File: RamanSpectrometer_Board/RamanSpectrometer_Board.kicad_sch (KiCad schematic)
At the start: 35 parts, among them J1 RJ45_LED_Shielded, Q1 BSS138, Q2 BSS138, Q3 BSS138, Q4 BSS138, Q5 BSS138, U1 Teensy4.1_DEV-16771, U2 OKI, U3 OKI

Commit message: footprints
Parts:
- C2, C3, C4, C5: footprint (none) -> Capacitor_SMD:C_0603_1608Metric_Pad1.08x0.95mm_HandSolder
- Conn1: footprint (none) -> MRDT_Connectors:Square_Anderson_2_H_Side_By_Side_PV
- Conn2, Conn4: footprint (none) -> MRDT_Connectors:MOLEX_SL_05_Vertical
- Conn3: footprint (none) -> MRDT_Connectors:MOLEX_SL_03_Vertical
- Conn5: footprint (none) -> MRDT_Connectors:MOLEX_SL_02_Vertical
- D1, D2, D3: footprint (none) -> LED_SMD:LED_0603_1608Metric_Pad1.05x0.95mm_HandSolder
- J1: footprint (none) -> MRDT_Connectors:RJ45_Teensy
- R1, R10, R2, R3, R5, R6, R8: footprint (none) -> Resistor_SMD:R_0603_1608Metric_Pad0.98x0.95mm_HandSolder
- U2, U3: footprint (none) -> MRDT_Devices:OKI_Horizontal
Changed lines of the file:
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@@
 			)
 		)
-		(property "Footprint" ""
+		(property "Footprint" "MRDT_Devices:OKI_Horizontal"
 			(at 66.04 35.56 0)
 			(effects
@@
 			)
 		)
-		(property "Footprint" ""
+		(property "Footprint" "Resistor_SMD:R_0603_1608Metric_Pad0.98x0.95mm_HandSolder"
 			(at 171.45 80.518 90)
 			(effects
@@
 			)
 		)
-		(property "Footprint" ""
+		(property "Footprint" "MRDT_Devices:OKI_Horizontal"
 			(at 120.65 168.91 0)
 			(effects
@@
 			)
 		)
-		(property "Footprint" ""
+		(property "Footprint" "LED_SMD:LED_0603_1608Metric_Pad1.05x0.95mm_HandSolder"
 			(at 128.27 36.83 0)
 			(effects
@@
 			)
 		)
-		(property "Footprint" ""
+		(property "Footprint" "Capacitor_SMD:C_0603_1608Metric_Pad1.08x0.95mm_HandSolder"
 			(at 145.7452 172.72 0)
 			(effects
@@
 			)
 		)
-		(property "Footprint" ""
+		(property "Footprint" "Resistor_SMD:R_0603_1608Metric_Pad0.98x0.95mm_HandSolder"
 			(at 130.81 80.518 90)
 			(effects
@@
 			)
 		)
-		(property "Footprint" ""
+		(property "Footprint" "Capacitor_SMD:C_0603_1608Metric_Pad1.08x0.95mm_HandSolder"
 			(at 63.1952 39.37 0)
 			(effects
@@
 			)
 		)
-		(property "Footprint" ""
+		(property "Footprint" "MRDT_Connectors:MOLEX_SL_03_Vertical"
 			(at 130.81 134.62 0)
 			(effects
@@
 			)
 		)
-		(property "Footprint" ""
+		(property "Footprint" "Resistor_SMD:R_0603_1608Metric_Pad0.98x0.95mm_HandSolder"
 			(at 116.332 49.53 90)
 			(effects
@@
 			)
 		)
-		(property "Footprint" ""
+		(property "Footprint" "MRDT_Connectors:RJ45_Teensy"
 			(at 234.95 34.925 90)
 			(effects
@@
 			)
 		)
-		(property "Footprint" ""
+		(property "Footprint" "Resistor_SMD:R_0603_1608Metric_Pad0.98x0.95mm_HandSolder"
 			(at 136.652 49.53 90)
 			(effects
@@
 			)
 		)
-		(property "Footprint" ""
+		(property "Footprint" "MRDT_Connectors:MOLEX_SL_05_Vertical"
 			(at 180.34 43.18 0)
 			(effects
@@
 			)
 		)
-		(property "Footprint" ""
+		(property "Footprint" "Capacitor_SMD:C_0603_1608Metric_Pad1.08x0.95mm_HandSolder"
 			(at 117.8052 172.72 0)
 			(effects
@@
 			)
 		)
-		(property "Footprint" ""
+		(property "Footprint" "LED_SMD:LED_0603_1608Metric_Pad1.05x0.95mm_HandSolder"
 			(at 138.43 36.83 0)
 			(effects
@@
 			)
 		)
-		(property "Footprint" ""
+		(property "Footprint" "MRDT_Connectors:Square_Anderson_2_H_Side_By_Side_PV"
 			(at 20.32 53.34 0)
 			(effects
@@
 			)
 		)
-		(property "Footprint" ""
+		(property "Footprint" "MRDT_Connectors:MOLEX_SL_02_Vertical"
 			(at 220.98 120.65 0)
 			(effects
@@
 			)
 		)
-		(property "Footprint" ""
+		(property "Footprint" "MRDT_Connectors:MOLEX_SL_05_Vertical"
 			(at 180.34 138.43 0)
 			(effects
@@
 			)
 		)
-		(property "Footprint" ""
+		(property "Footprint" "MRDT_Connectors:Square_Anderson_2_H_Side_By_Side_PV"
 			(at 20.32 43.18 0)
 			(effects
@@
 			)
 		)
-		(property "Footprint" ""
+		(property "Footprint" "Resistor_SMD:R_0603_1608Metric_Pad0.98x0.95mm_HandSolder"
 			(at 126.492 49.53 90)
 			(effects
@@
 			)
 		)
-		(property "Footprint" ""
+		(property "Footprint" "Resistor_SMD:R_0603_1608Metric_Pad0.98x0.95mm_HandSolder"
 			(at 219.71 86.868 90)
 			(effects
@@
 			)
 		)
-		(property "Footprint" ""
+		(property "Footprint" "Resistor_SMD:R_0603_1608Metric_Pad0.98x0.95mm_HandSolder"
 			(at 250.19 86.868 90)
 			(effects
@@
 			)
 		)
-		(property "Footprint" ""
+		(property "Footprint" "Capacitor_SMD:C_0603_1608Metric_Pad1.08x0.95mm_HandSolder"
 			(at 91.1352 39.37 0)
 			(effects
@@
 			)
 		)
-		(property "Footprint" ""
+		(property "Footprint" "LED_SMD:LED_0603_1608Metric_Pad1.05x0.95mm_HandSolder"
 			(at 118.11 36.83 0)
 			(effects

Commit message: PCB Holes
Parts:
- H1, H2, H3, H4: footprint (none) -> MountingHole:MountingHole_3.2mm_M3
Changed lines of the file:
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@@
 			)
 		)
-		(property "Footprint" ""
+		(property "Footprint" "MountingHole:MountingHole_3.2mm_M3"
 			(at 269.24 24.13 0)
 			(effects
@@
 			)
 		)
-		(property "Footprint" ""
+		(property "Footprint" "MountingHole:MountingHole_3.2mm_M3"
 			(at 275.59 31.75 0)
 			(effects
@@
 			)
 		)
-		(property "Footprint" ""
+		(property "Footprint" "MountingHole:MountingHole_3.2mm_M3"
 			(at 269.24 31.75 0)
 			(effects
@@
 			)
 		)
-		(property "Footprint" ""
+		(property "Footprint" "MountingHole:MountingHole_3.2mm_M3"
 			(at 275.59 24.13 0)
 			(effects

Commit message: pcb routing
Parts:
- Conn2: value Molex_SL_05 -> Gantry
- Conn3: value Molex_SL_03 -> Diode
- Conn4: value Molex_SL_05 -> CCD
- U2: value OKI -> OKI 12V-5V
- U3: value OKI -> OKI 5V-3V
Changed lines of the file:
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@@
 			)
 		)
-		(property "Value" "OKI"
+		(property "Value" "OKI 12V-5V"
 			(at 76.2 25.4 0)
 			(effects
@@
 			)
 		)
-		(property "Value" "OKI"
+		(property "Value" "OKI 5V-3V"
 			(at 130.81 158.75 0)
 			(effects
@@
 			)
 		)
-		(property "Value" "Molex_SL_03"
+		(property "Value" "Diode"
 			(at 134.62 132.0799 0)
 			(effects
@@
 			)
 		)
-		(property "Value" "Molex_SL_05"
+		(property "Value" "CCD"
 			(at 184.15 38.0999 0)
 			(effects
@@
 			)
 		)
-		(property "Value" "Molex_SL_05"
+		(property "Value" "Gantry"
 			(at 184.15 133.3499 0)
 			(effects

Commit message: PCB rough draft
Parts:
- Conn5: value Molex_SL_02 -> Fan
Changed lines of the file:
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@@
 			)
 		)
-		(property "Value" "Molex_SL_02"
+		(property "Value" "Fan"
 			(at 219.71 120.65 0)
 			(effects

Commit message: PCB Raman edit and TOF
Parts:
- added U4: VL53L4CX, Connector_PinSocket_2.54mm:PinSocket_1x06_P2.54mm_Vertical, symbol MRDT_Sensors:VL53L4CX
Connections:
- net +3.3V: now also U4.1 (VIN)
- net GND: now also U4.2 (GND)
- net SDA: now reaches U1.18 (A4)
- net SDA: now also U4.4 (SDA)
- net SCL: now reaches U1.19 (A5)
- net SCL: now also U4.3 (SCL)
- no-connect marks 40 -> 38

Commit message: ihateyoujesse
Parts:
- removed D4: 782nm Laser Diode, symbol Device:LED
- removed D5: 520nm Laser Diode, symbol Device:LED
- removed Q3, Q4: BSS138, Package_TO_SOT_SMD:SOT-23, symbol Transistor_FET:BSS138
- removed R10: 33, Resistor_SMD:R_0603_1608Metric_Pad0.98x0.95mm_HandSolder, symbol Device:R
- removed R8: 78.7, Resistor_SMD:R_0603_1608Metric_Pad0.98x0.95mm_HandSolder, symbol Device:R
- removed U4: VL53L4CX, Connector_PinSocket_2.54mm:PinSocket_1x06_P2.54mm_Vertical, symbol MRDT_Sensors:VL53L4CX
- added U4: VL53L4CX, VL53L4CX:VL53L4CX, symbol vl53l4cx:VL53L4CX
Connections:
- net +3.3V: now also U4.1 (VIN)
- net GND: now also U4.2 (GND)
- net SCL: now also U4.3 (SCL)
- net SDA: now also U4.4 (SDA)
- net GPIO: now reaches U1.17 (A3)
- net GPIO: now also U4.5 (GPIO)
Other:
- note removed: "Diodes"

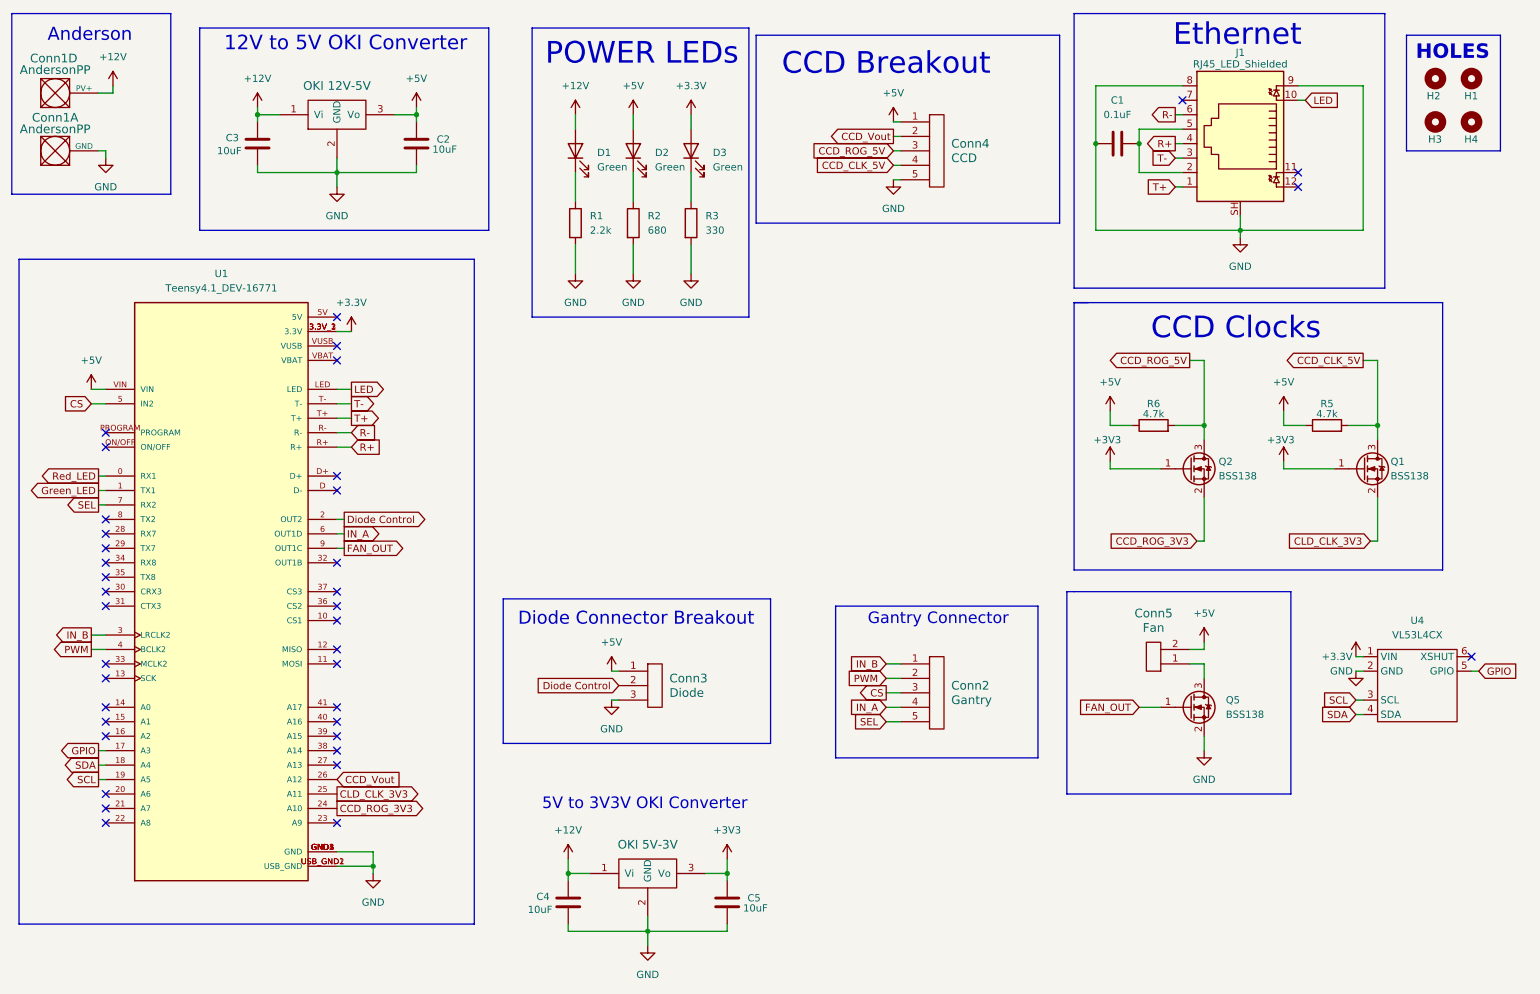
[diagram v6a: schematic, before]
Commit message: Raman PCB Additions
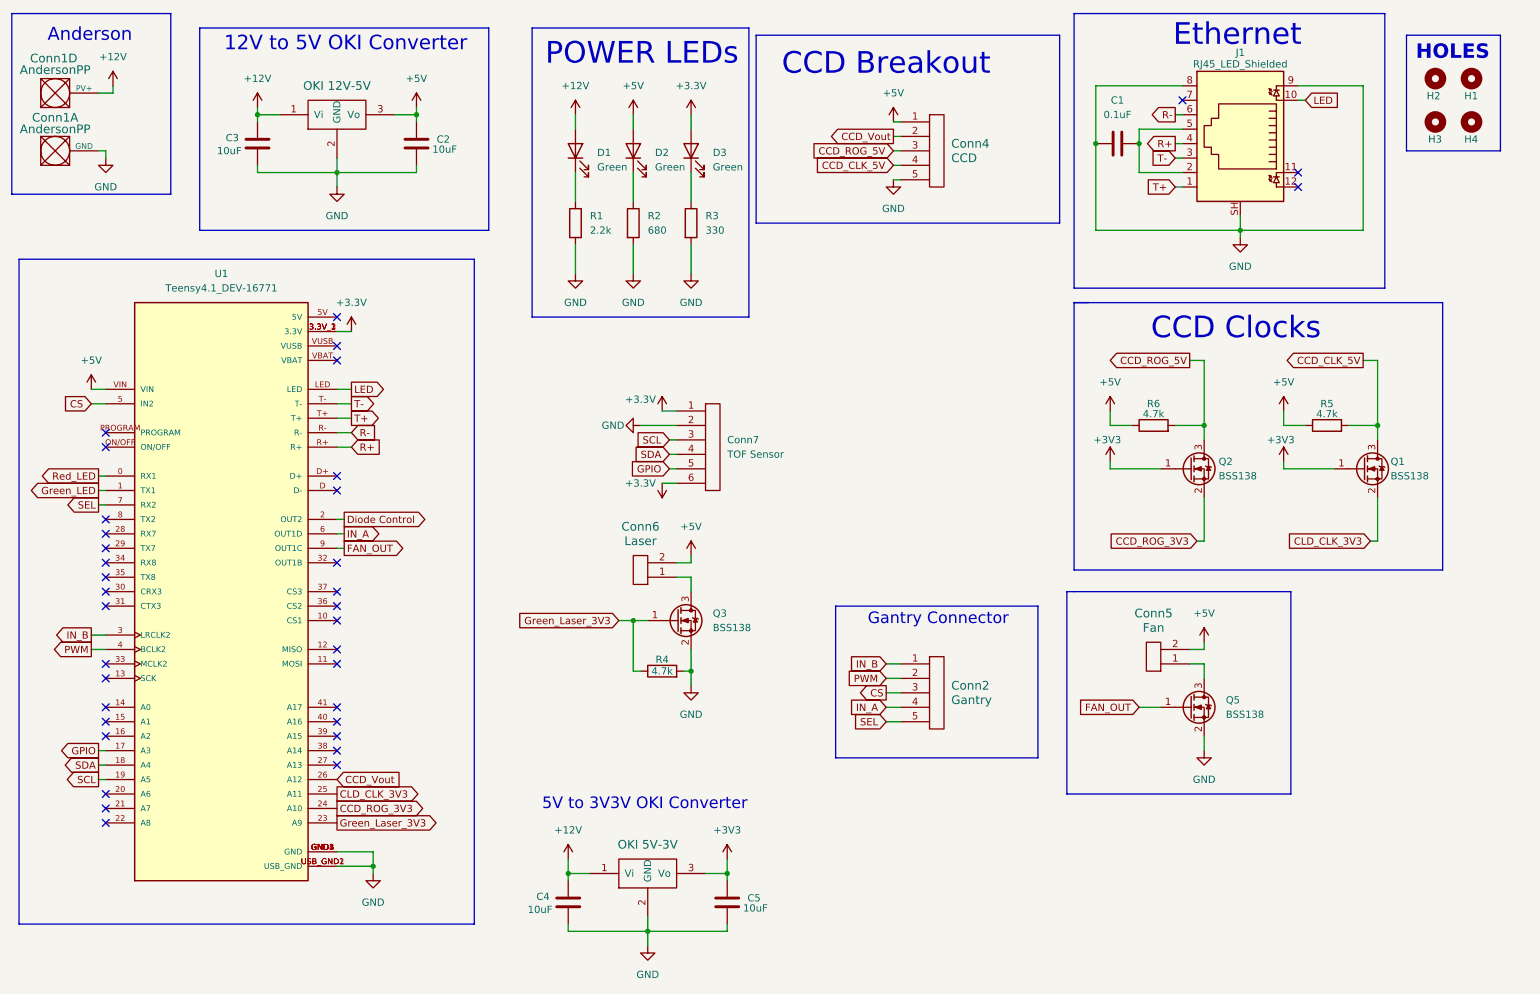
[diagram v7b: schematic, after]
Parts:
- removed Conn3: Diode, MRDT_Connectors:MOLEX_SL_03_Vertical, symbol MRDT_Connectors:Molex_SL_03
- removed U4: VL53L4CX, VL53L4CX:VL53L4CX, symbol vl53l4cx:VL53L4CX
- added Conn6: Laser, MRDT_Connectors:MOLEX_SL_02_Vertical, symbol MRDT_Connectors:Molex_SL_02
- added Conn7: TOF Sensor, MRDT_Connectors:MOLEX_SL_06_Vertical, symbol MRDT_Connectors:Molex_SL_06
- added Q3: BSS138, Package_TO_SOT_SMD:SOT-23, symbol Transistor_FET:BSS138
- added R4: 4.7k, Resistor_SMD:R_0603_1608Metric_Pad0.98x0.95mm_HandSolder, symbol Device:R
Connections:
- net +3.3V: now also Conn7.1, Conn7.6
- net +5V: now also Conn6.2
- net GND: now also Conn7.2, Q3.2 (S), R4.2
- net GPIO: now also Conn7.5
- net SCL: now also Conn7.3
- net SDA: now also Conn7.4
- net Green_Laser_3V3: now reaches U1.23 (A9)
- net Green_Laser_3V3: now also Q3.1 (G), R4.1
- new net: Conn6.1, Q3.3 (D)
- no-connect marks 38 -> 36
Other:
- note removed: "Diode Connector Breakout"

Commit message: Schematic Changes
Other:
- note added: "Diode Connector"
- note added: "Fan Connector"
- note added: "TOF Sensor"
- moved on the sheet: C4, C5, Conn2, Conn4, Conn5, Conn6, Conn7, Q3, Q5, R4
